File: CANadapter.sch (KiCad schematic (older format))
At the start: 27 parts, among them P1 CONN_02X06, P2 CONN_01X06, P3 CONN_01X04, P4 CONN_01X06, U1 MCP2515, U2 TLP2361, U3 TLP2361, U4 MCP2551-I/SN, U5 LM7805CT, Y1 16MHz

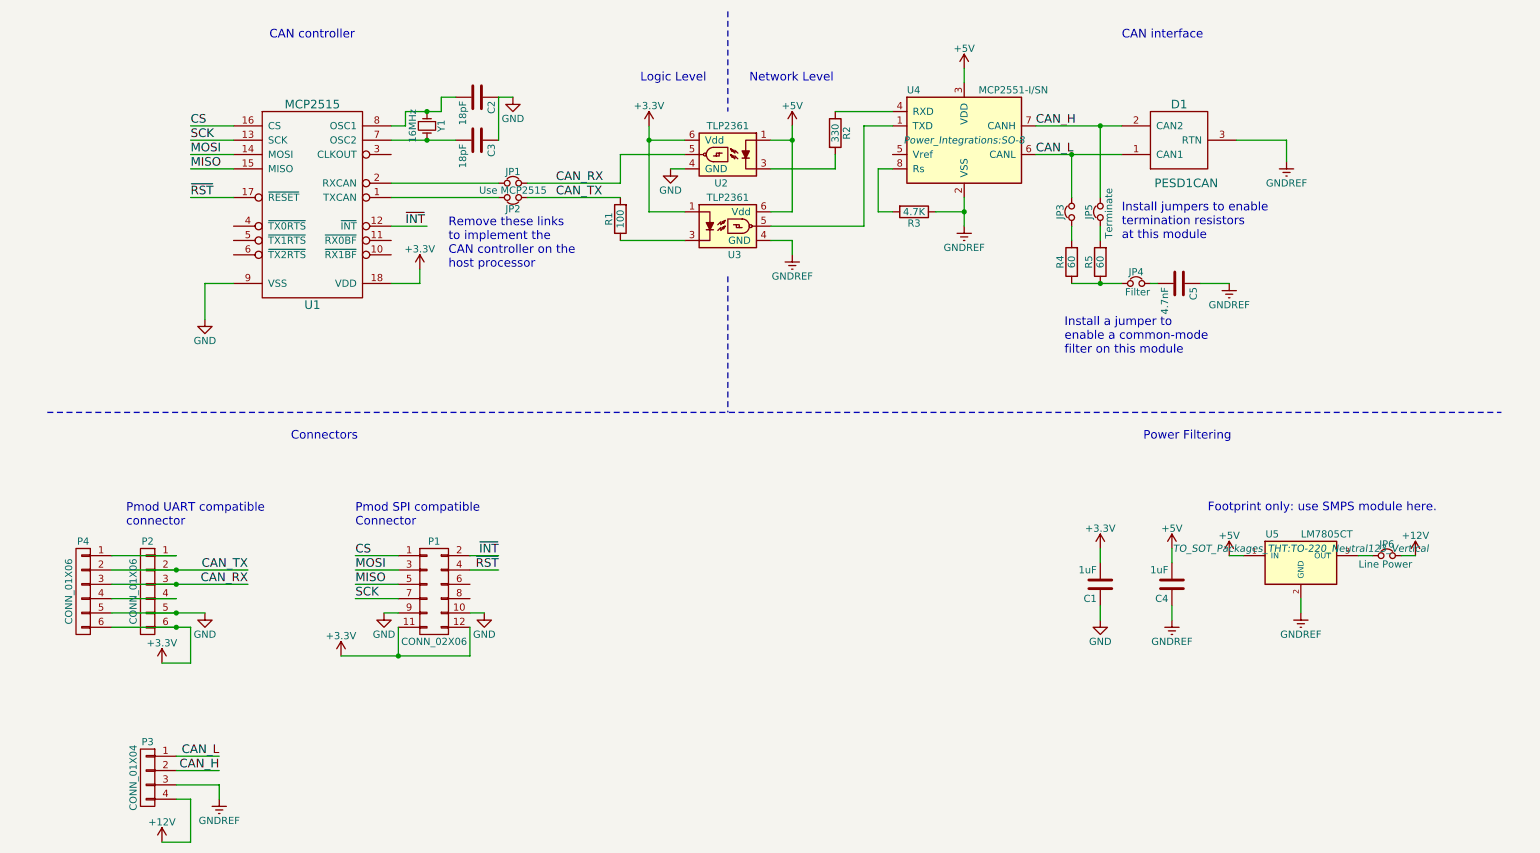
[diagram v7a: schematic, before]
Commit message: added isolating smps, moved jumpers, added ground pours
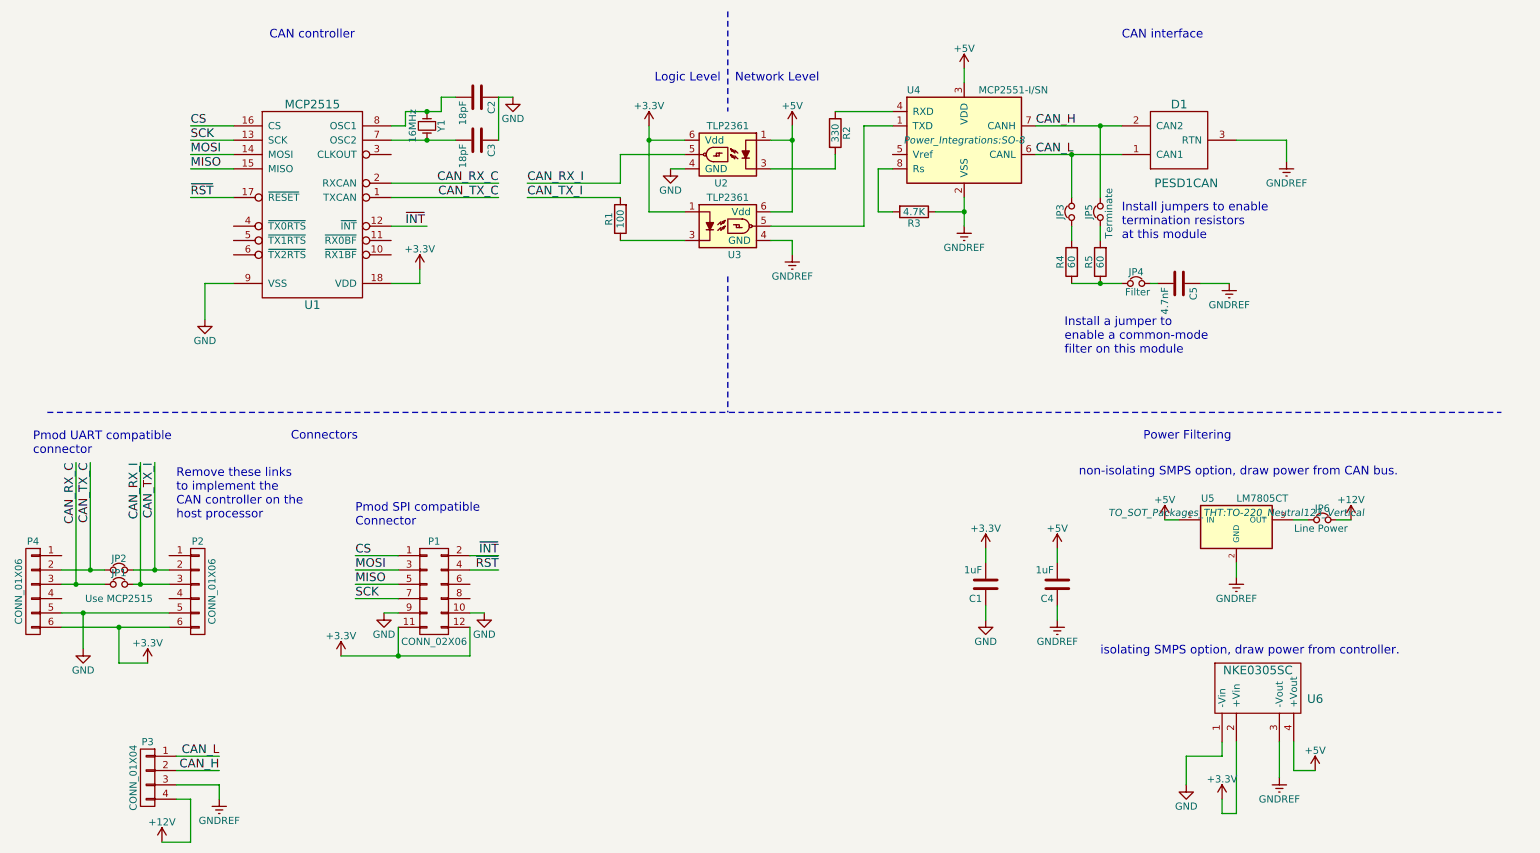
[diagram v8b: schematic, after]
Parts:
- added U6: NKE0305SC, LocalLib:Murata_SIL, symbol NKE0305SC
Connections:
- net +3V3: now also U6.2 (+Vin)
- net +5V: now also U6.4 (+Vout)
- net GND: now also U6.1 (-Vin)
- net GNDREF: now also U6.3 (-Vout)
- net CAN_TX_C: now reaches JP2.1, U1.1 (TXCAN)
- net CAN_TX_C: now also P4.2 (P2)
- net CAN_RX_C: now reaches JP1.1, U1.2 (RXCAN)
- net CAN_RX_C: now also P4.3 (P3)
- net at P2.1 (P1): no longer P4.1 (P1)
- net at P2.4 (P4): no longer P4.4 (P4)
- net CAN_RX renamed CAN_RX_I
- net CAN_RX_I: no longer P4.3 (P3)
- net CAN_TX renamed CAN_TX_I
- net CAN_TX_I: no longer P4.2 (P2)
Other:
- note added: "isolating SMPS option, draw power from controller."
- note added: "non-isolating SMPS option, draw power from CAN bus."
- note removed: "Footprint only: use SMPS module here."
- moved on the sheet: C1, C4, JP1, JP2, JP6, P2, P4, U5
